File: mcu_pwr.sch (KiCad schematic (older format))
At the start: 26 parts, among them P4 CONN_2, P5 KNUSB, U4 STM32F40X_LQFP64, U6 LP38691, X1 CRYSTAL

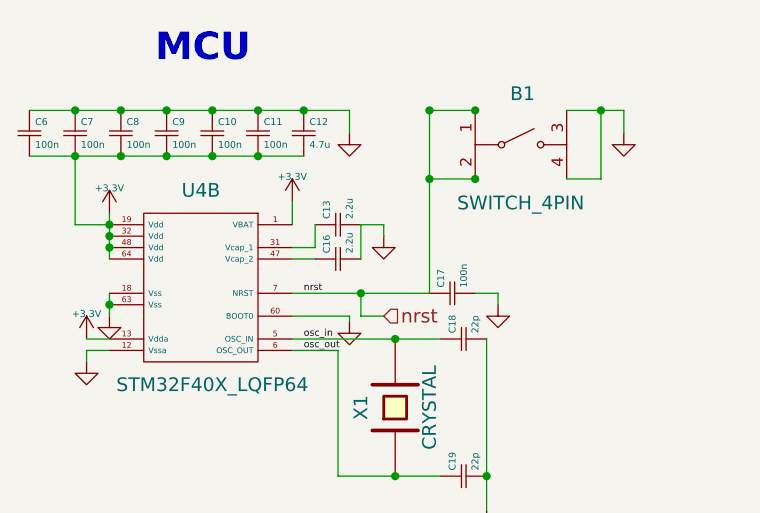
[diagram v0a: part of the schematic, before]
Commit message: LED routing, and initial placement of most remaining components.
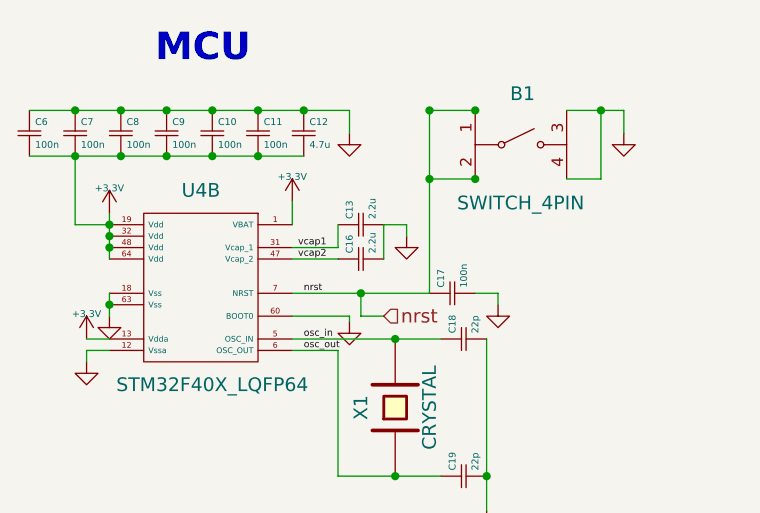
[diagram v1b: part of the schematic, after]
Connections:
- net labels added: vcap1, vcap2
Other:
- moved on the sheet: C13, C16
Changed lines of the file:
@@
 $EndComp
 Wire Wire Line
-	2400 1850 2500 1850
+	2400 1850 2600 1850
 $Comp
 L Csmall C16
 U 1 1 54A99019
-P 2600 1850
-F 0 "C16" H 2625 1900 30  0000 L CNN
-F 1 "2.2u" H 2625 1800 30  0000 L CNN
-F 2 "" H 2600 1850 60  0000 C CNN
-F 3 "" H 2600 1850 60  0000 C CNN
-	1    2600 1850
+P 2700 1850
+F 0 "C16" H 2725 1900 30  0000 L CNN
+F 1 "2.2u" H 2725 1800 30  0000 L CNN
+F 2 "" H 2700 1850 60  0000 C CNN
+F 3 "" H 2700 1850 60  0000 C CNN
+	1    2700 1850
 	0    -1   -1   0
 $EndComp
@@
 L Csmall C13
 U 1 1 54A9901F
-P 2600 1700
-F 0 "C13" H 2625 1750 30  0000 L CNN
-F 1 "2.2u" H 2625 1650 30  0000 L CNN
-F 2 "" H 2600 1700 60  0000 C CNN
-F 3 "" H 2600 1700 60  0000 C CNN
-	1    2600 1700
-	0    -1   -1   0
-$EndComp
-Wire Wire Line
-	2400 1800 2500 1800
-Wire Wire Line
-	2500 1800 2500 1700
-Wire Wire Line
-	2700 1850 2700 1700
-Wire Wire Line
-	2700 1700 2800 1700
-Wire Wire Line
-	2800 1700 2800 1750
+P 2700 1700
+F 0 "C13" H 2725 1750 30  0000 L CNN
+F 1 "2.2u" H 2725 1650 30  0000 L CNN
+F 2 "" H 2700 1700 60  0000 C CNN
+F 3 "" H 2700 1700 60  0000 C CNN
+	1    2700 1700
+	0    -1   -1   0
+$EndComp
+Wire Wire Line
+	2400 1800 2600 1800
+Wire Wire Line
+	2600 1800 2600 1700
+Wire Wire Line
+	2800 1850 2800 1700
+Wire Wire Line
+	2800 1700 2900 1700
+Wire Wire Line
+	2900 1700 2900 1750
 $Comp
 L GND #PWR021
 U 1 1 54A9902A
-P 2800 1750
-F 0 "#PWR021" H 2800 1750 30  0001 C CNN
-F 1 "GND" H 2800 1680 30  0001 C CNN
-F 2 "" H 2800 1750 60  0000 C CNN
-F 3 "" H 2800 1750 60  0000 C CNN
-	1    2800 1750
+P 2900 1750
+F 0 "#PWR021" H 2900 1750 30  0001 C CNN
+F 1 "GND" H 2900 1680 30  0001 C CNN
+F 2 "" H 2900 1750 60  0000 C CNN
+F 3 "" H 2900 1750 60  0000 C CNN
+	1    2900 1750
 	1    0    0    -1
 $EndComp
@@
 LED indication
 Connection ~ 3000 1500
+Text Label 2425 1800 0    30   ~ 0
+vcap1
+Text Label 2425 1850 0    30   ~ 0
+vcap2
 $EndSCHEMATC

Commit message: Routing
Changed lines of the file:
@@
 	-1   0    0    1
 $EndComp
-Text HLabel 2750 4650 2    60   BiDi ~ 0
+Text HLabel 2750 4850 2    60   BiDi ~ 0
 usb_id
 Text HLabel 2750 4750 2    60   BiDi ~ 0
 usb_dp
-Text HLabel 2750 4850 2    60   BiDi ~ 0
+Text HLabel 2750 4650 2    60   BiDi ~ 0
 usb_dm
 Text HLabel 5250 4550 0    60   Input ~ 0

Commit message: Complete routing
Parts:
- C10, C11, C12, C13, C16, C17, C18, C19, C6, C7, C8, C9: footprint (none) -> w_smd_cap:c_0805
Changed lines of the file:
@@
 F 0 "C16" H 2725 1900 30  0000 L CNN
 F 1 "2.2u" H 2725 1800 30  0000 L CNN
-F 2 "" H 2700 1850 60  0000 C CNN
+F 2 "w_smd_cap:c_0805" H 2700 1850 60  0001 C CNN
 F 3 "" H 2700 1850 60  0000 C CNN
 	1    2700 1850
@@
 F 0 "C13" H 2725 1750 30  0000 L CNN
 F 1 "2.2u" H 2725 1650 30  0000 L CNN
-F 2 "" H 2700 1700 60  0000 C CNN
+F 2 "w_smd_cap:c_0805" H 2700 1700 60  0001 C CNN
 F 3 "" H 2700 1700 60  0000 C CNN
 	1    2700 1700
@@
 F 0 "C17" H 3125 2050 30  0000 L CNN
 F 1 "100n" H 3125 1950 30  0000 L CNN
-F 2 "" H 3100 2000 60  0001 C CNN
+F 2 "w_smd_cap:c_0805" H 3100 2000 60  0001 C CNN
 F 3 "" H 3100 2000 60  0001 C CNN
 	1    3100 2000
@@
 F 0 "C19" H 3175 2850 30  0000 L CNN
 F 1 "22p" H 3175 2750 30  0000 L CNN
-F 2 "" H 3150 2800 60  0001 C CNN
+F 2 "w_smd_cap:c_0805" H 3150 2800 60  0001 C CNN
 F 3 "" H 3150 2800 60  0001 C CNN
 	1    3150 2800
@@
 F 0 "C18" H 3175 2250 30  0000 L CNN
 F 1 "22p" H 3175 2150 30  0000 L CNN
-F 2 "" H 3150 2200 60  0001 C CNN
+F 2 "w_smd_cap:c_0805" H 3150 2200 60  0001 C CNN
 F 3 "" H 3150 2200 60  0001 C CNN
 	1    3150 2200
@@
 F 0 "C7" H 1475 1350 30  0000 L CNN
 F 1 "100n" H 1475 1250 30  0000 L CNN
-F 2 "" H 1450 1300 60  0000 C CNN
+F 2 "w_smd_cap:c_0805" H 1450 1300 60  0001 C CNN
 F 3 "" H 1450 1300 60  0000 C CNN
 	1    1450 1300
@@
 F 0 "C8" H 1675 1350 30  0000 L CNN
 F 1 "100n" H 1675 1250 30  0000 L CNN
-F 2 "" H 1650 1300 60  0000 C CNN
+F 2 "w_smd_cap:c_0805" H 1650 1300 60  0001 C CNN
 F 3 "" H 1650 1300 60  0000 C CNN
 	1    1650 1300
@@
 F 0 "C9" H 1875 1350 30  0000 L CNN
 F 1 "100n" H 1875 1250 30  0000 L CNN
-F 2 "" H 1850 1300 60  0000 C CNN
+F 2 "w_smd_cap:c_0805" H 1850 1300 60  0001 C CNN
 F 3 "" H 1850 1300 60  0000 C CNN
 	1    1850 1300
@@
 F 0 "C10" H 2075 1350 30  0000 L CNN
 F 1 "100n" H 2075 1250 30  0000 L CNN
-F 2 "" H 2050 1300 60  0000 C CNN
+F 2 "w_smd_cap:c_0805" H 2050 1300 60  0001 C CNN
 F 3 "" H 2050 1300 60  0000 C CNN
 	1    2050 1300
@@
 F 0 "C11" H 2275 1350 30  0000 L CNN
 F 1 "100n" H 2275 1250 30  0000 L CNN
-F 2 "" H 2250 1300 60  0000 C CNN
+F 2 "w_smd_cap:c_0805" H 2250 1300 60  0001 C CNN
 F 3 "" H 2250 1300 60  0000 C CNN
 	1    2250 1300
@@
 F 0 "C12" H 2475 1350 30  0000 L CNN
 F 1 "4.7u" H 2475 1250 30  0000 L CNN
-F 2 "" H 2450 1300 60  0000 C CNN
+F 2 "w_smd_cap:c_0805" H 2450 1300 60  0001 C CNN
 F 3 "" H 2450 1300 60  0000 C CNN
 	1    2450 1300
@@
 F 0 "C6" H 1275 1350 30  0000 L CNN
 F 1 "100n" H 1275 1250 30  0000 L CNN
-F 2 "" H 1250 1300 60  0000 C CNN
+F 2 "w_smd_cap:c_0805" H 1250 1300 60  0001 C CNN
 F 3 "" H 1250 1300 60  0000 C CNN
 	1    1250 1300

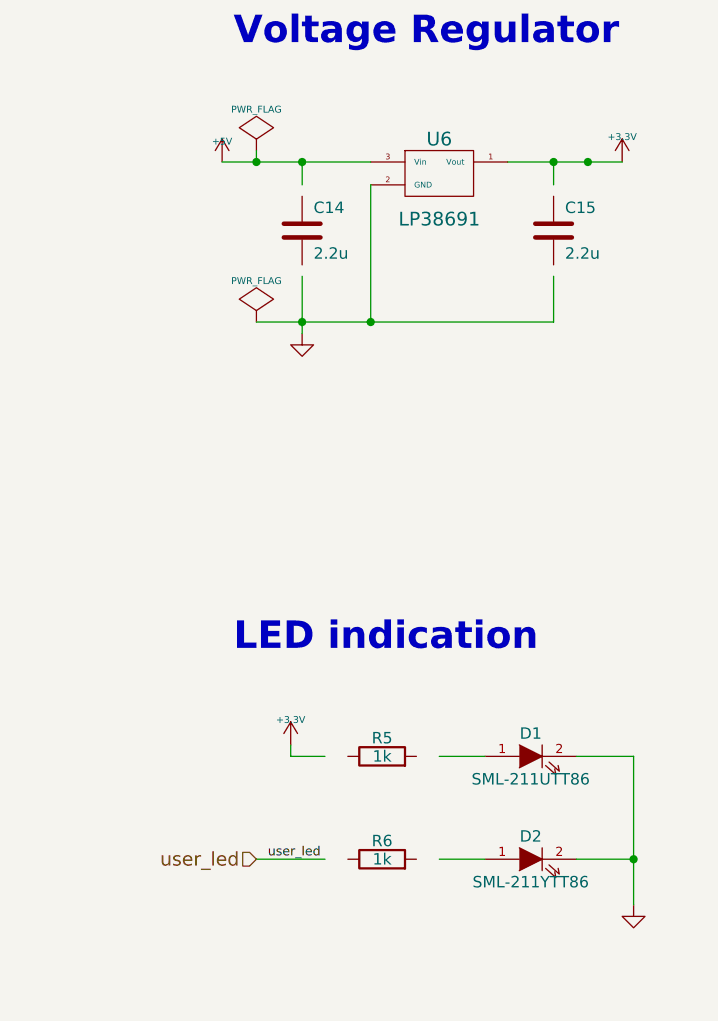
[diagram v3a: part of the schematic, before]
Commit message: Fixup some missing wires after kicad upgrade
(A resistor and a capacitor component now has shorter leads, it seems.
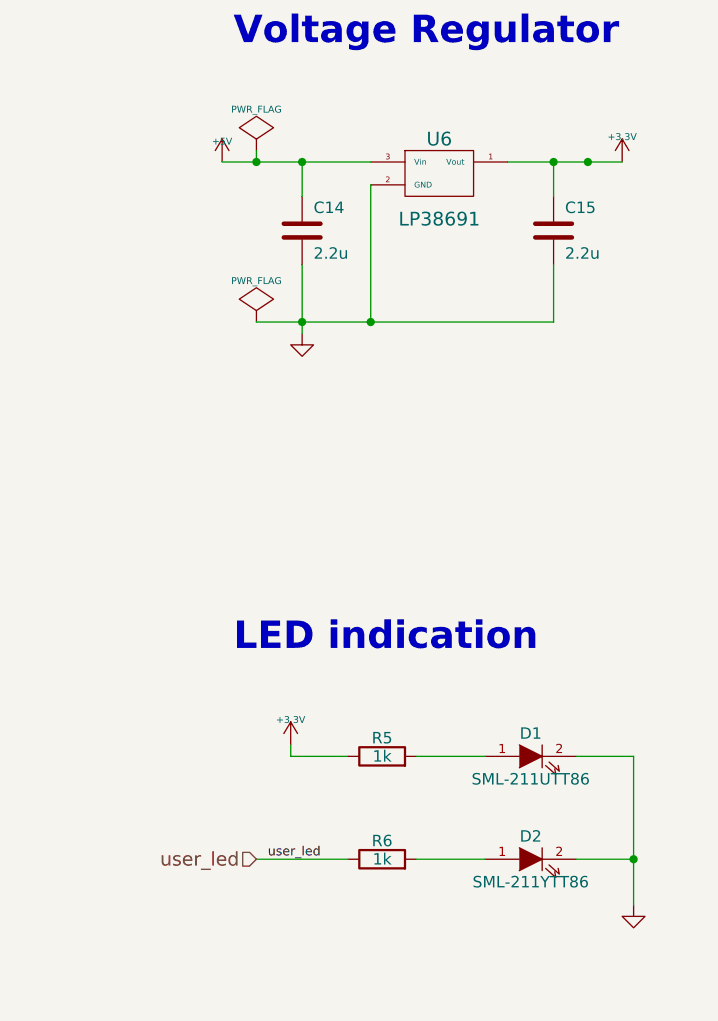
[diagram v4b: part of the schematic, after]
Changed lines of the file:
@@
 Connection ~ 6550 1500
 Wire Wire Line
-	6550 1600 6550 1500
+	6550 1650 6550 1500
 Connection ~ 5450 2200
 Wire Wire Line
-	5450 2000 5450 2250
+	5450 1950 5450 2250
 Wire Wire Line
 	5100 1500 5750 1500
@@
 	6350 1500 6850 1500
 Wire Wire Line
-	5450 1600 5450 1500
+	5450 1650 5450 1500
 Connection ~ 5450 1500
 Wire Wire Line
@@
 	5250 2200 6550 2200
 Wire Wire Line
-	6550 2200 6550 2000
+	6550 2200 6550 1950
 Wire Wire Line
 	5750 1600 5750 2200
@@
 	5400 4050 5400 4100
 Wire Wire Line
-	5400 4100 5550 4100
+	5400 4100 5650 4100
 Wire Wire Line
-	6050 4100 6250 4100
+	5950 4100 6250 4100
 Wire Wire Line
 	6900 4100 6900 4750
@@
 Connection ~ 6900 4550
 Wire Wire Line
-	6050 4550 6250 4550
+	5950 4550 6250 4550
 Wire Wire Line
-	5250 4550 5550 4550
+	5250 4550 5650 4550
 Text Label 5300 4550 0    40   ~ 0
 user_led
